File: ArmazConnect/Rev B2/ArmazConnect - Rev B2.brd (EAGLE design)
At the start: 165 x 74 mm, 37 parts, among them X0 NC3FAAV2, X1 NC3FAAV2, X2 NC3FAAV2, X3 NC3FAAV2, X4 NC5FAV-SW, X5 NC5MAV-SW, X6 NC5FAV-SW, X8 87832-26

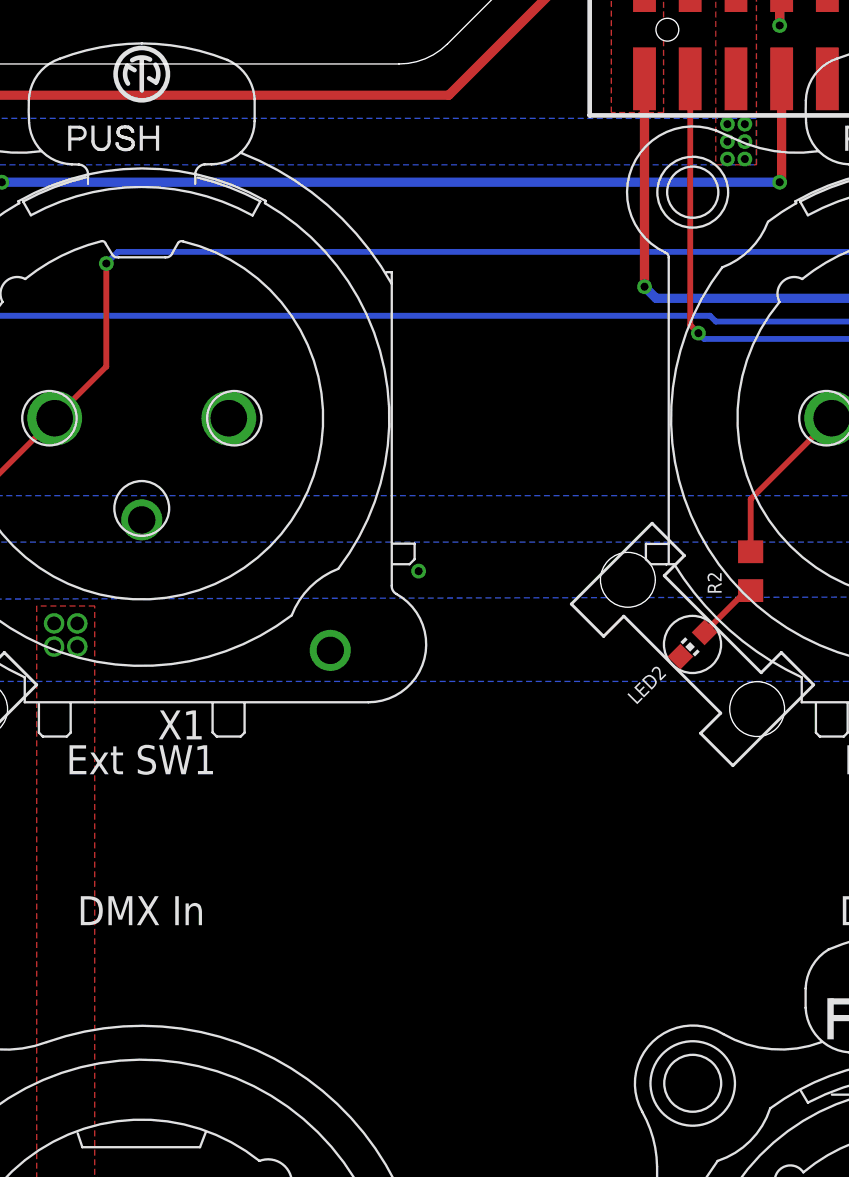
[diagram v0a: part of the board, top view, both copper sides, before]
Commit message: Update ArmazConnect - Rev B2 schematic and board, add two dc/dc converter (12V/5V) in parallel
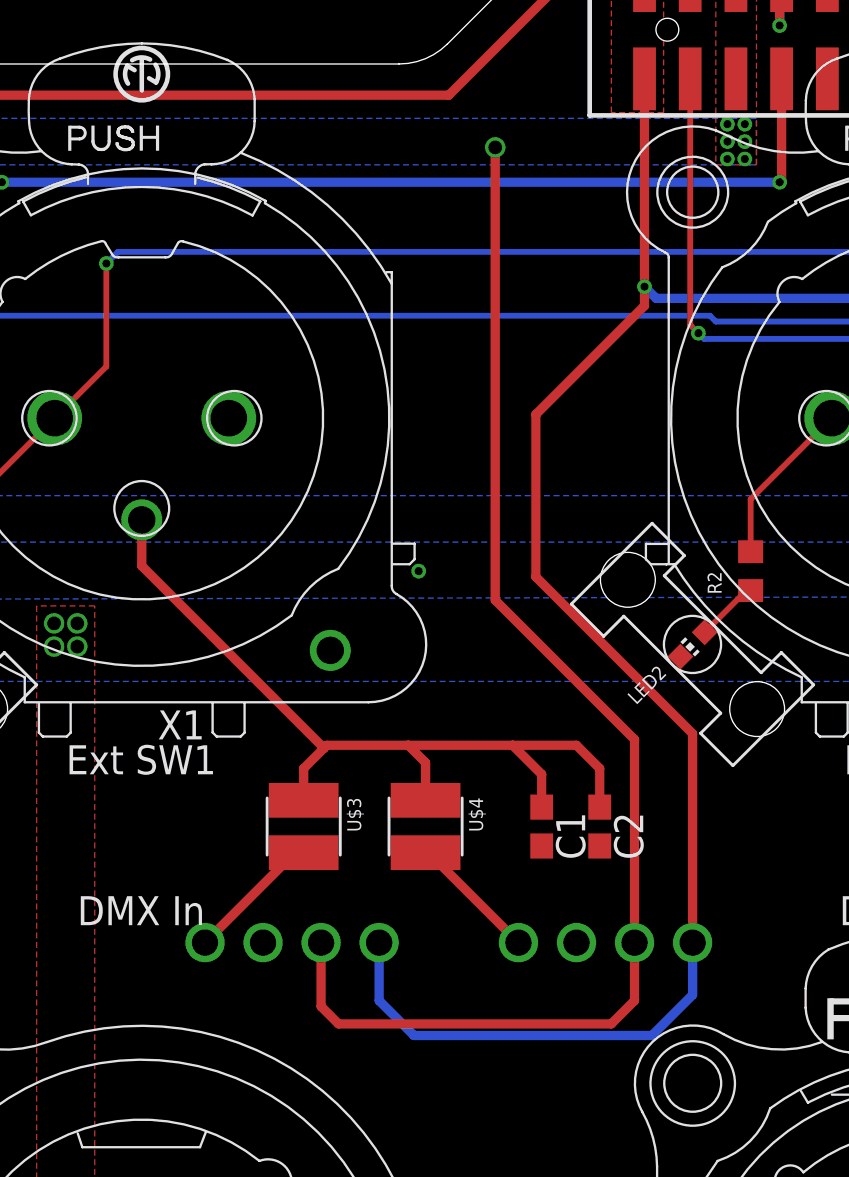
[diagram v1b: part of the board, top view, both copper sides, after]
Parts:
- added C1, C2: 4.7uF, rcl:C0603
- added U$1, U$2: MEE3S1205SC, dc-dc-converter:MEE3
- added U$3, U$4: 10uH, murata-inductance:8200
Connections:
- new net N$5: U$1.4, U$3.1
- new net N$7: U$2.4, U$4.1
- net +12V: now also U$1.2, U$2.2
- net +5V: now also C1.1, C2.1, U$3.2, U$4.2
- net GND: now also C1.2, C2.2, U$1.3, U$2.3
- net GND1: now also U$1.1, U$2.1
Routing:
- net +12V: track 0.00 -> 57.1 mm, vias 6 -> 7
- net GND1: track 79.3 -> 132.7 mm
- net +5V: track 33.5 -> 69.6 mm
- net N$5: track 0.00 -> 5.95 mm
- net N$7: track 0.00 -> 5.69 mm
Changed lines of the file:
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@@
 <attribute name="VALUE" x="136.906" y="57.912" size="0.4064" layer="27" ratio="10"/>
 </element>
+<element name="U$1" library="dc-dc-converter" package="MEE3" value="MEE3S1205SC" x="48.768" y="35.052" rot="MR0"/>
+<element name="U$2" library="dc-dc-converter" package="MEE3" value="MEE3S1205SC" x="62.484" y="35.052" rot="MR0"/>
+<element name="U$3" library="murata-inductance" package="8200" value="10uH" x="53.086" y="40.132" rot="R180"/>
+<element name="U$4" library="murata-inductance" package="8200" value="10uH" x="58.42" y="40.132" rot="R180"/>
+<element name="C1" library="rcl" package="C0603" value="4.7uF" x="63.5" y="40.132" rot="R270"/>
+<element name="C2" library="rcl" package="C0603" value="4.7uF" x="66.04" y="40.132" rot="R270"/>
 </elements>
 <signals>
@@
 <via x="118" y="45" extent="1-16" drill="0.35"/>
 <via x="135" y="45" extent="1-16" drill="0.35"/>
+<contactref element="C1" pad="2"/>
+<contactref element="C2" pad="2"/>
+<contactref element="U$2" pad="3"/>
+<contactref element="U$1" pad="3"/>
 </signal>
 <signal name="N$27">
@@
 <wire x1="137.414" y1="59.248" x2="137.8" y2="59.248" width="0.4064" layer="1"/>
 <wire x1="137.8" y1="59.248" x2="137.822" y2="59.27" width="0.4064" layer="1"/>
+<contactref element="U$3" pad="2"/>
+<contactref element="U$4" pad="2"/>
+<contactref element="C2" pad="1"/>
+<contactref element="C1" pad="1"/>
+<wire x1="53.086" y1="41.277" x2="53.086" y2="42.672" width="0.4064" layer="1"/>
+<wire x1="53.086" y1="42.672" x2="53.975" y2="43.561" width="0.4064" layer="1"/>
+<wire x1="53.975" y1="43.561" x2="54.102" y2="43.688" width="0.4064" layer="1"/>
+<wire x1="54.102" y1="43.688" x2="57.658" y2="43.688" width="0.4064" layer="1"/>
+<wire x1="57.658" y1="43.688" x2="62.23" y2="43.688" width="0.4064" layer="1"/>
+<wire x1="62.23" y1="43.688" x2="65.024" y2="43.688" width="0.4064" layer="1"/>
+<wire x1="65.024" y1="43.688" x2="66.04" y2="42.672" width="0.4064" layer="1"/>
+<wire x1="66.04" y1="42.672" x2="66.04" y2="40.982" width="0.4064" layer="1"/>
+<wire x1="63.5" y1="40.982" x2="63.5" y2="42.418" width="0.4064" layer="1"/>
+<wire x1="63.5" y1="42.418" x2="62.23" y2="43.688" width="0.4064" layer="1"/>
+<wire x1="58.42" y1="41.277" x2="58.42" y2="42.926" width="0.4064" layer="1"/>
+<wire x1="58.42" y1="42.926" x2="57.658" y2="43.688" width="0.4064" layer="1"/>
+<wire x1="46" y1="53.55" x2="46" y2="51.536" width="0.4064" layer="1"/>
+<wire x1="46" y1="51.536" x2="53.975" y2="43.561" width="0.4064" layer="1"/>
 </signal>
 <signal name="ESW0">
@@
 <via x="72.39" y="70.104" extent="1-16" drill="0.35" shape="square"/>
 <via x="71.628" y="70.104" extent="1-16" drill="0.35" shape="square"/>
+<contactref element="U$1" pad="2"/>
+<contactref element="U$2" pad="2"/>
+<wire x1="53.848" y1="35.052" x2="53.848" y2="32.258" width="0.4064" layer="1"/>
+<wire x1="53.848" y1="32.258" x2="54.61" y2="31.496" width="0.4064" layer="1"/>
+<wire x1="54.61" y1="31.496" x2="66.548" y2="31.496" width="0.4064" layer="1"/>
+<wire x1="66.548" y1="31.496" x2="67.564" y2="32.512" width="0.4064" layer="1"/>
+<wire x1="67.564" y1="32.512" x2="67.564" y2="35.052" width="0.4064" layer="1"/>
+<wire x1="67.564" y1="35.052" x2="67.564" y2="43.942" width="0.4064" layer="1"/>
+<wire x1="67.564" y1="43.942" x2="61.468" y2="50.038" width="0.4064" layer="1"/>
+<wire x1="61.468" y1="50.038" x2="61.468" y2="69.85" width="0.4064" layer="1"/>
+<via x="61.468" y="69.85" extent="1-16" drill="0.6" shape="square"/>
 </signal>
 <signal name="GND1" class="1">
@@
 <wire x1="68.508" y1="63.246" x2="68" y2="63.754" width="0.4064" layer="16"/>
 <via x="68" y="63.754" extent="1-16" drill="0.35"/>
+<contactref element="U$1" pad="1"/>
+<contactref element="U$2" pad="1"/>
+<wire x1="56.388" y1="35.052" x2="56.388" y2="32.512" width="0.4064" layer="16"/>
+<wire x1="56.388" y1="32.512" x2="57.912" y2="30.988" width="0.4064" layer="16"/>
+<wire x1="57.912" y1="30.988" x2="68.326" y2="30.988" width="0.4064" layer="16"/>
+<wire x1="68.326" y1="30.988" x2="70.104" y2="32.766" width="0.4064" layer="16"/>
+<wire x1="70.104" y1="32.766" x2="70.104" y2="35.052" width="0.4064" layer="16"/>
+<wire x1="70.104" y1="35.052" x2="70.104" y2="44.196" width="0.4064" layer="1"/>
+<wire x1="70.104" y1="44.196" x2="63.246" y2="51.054" width="0.4064" layer="1"/>
+<wire x1="63.246" y1="51.054" x2="63.246" y2="58.166" width="0.4064" layer="1"/>
+<wire x1="68" y1="63.754" x2="68" y2="62.92" width="0.4064" layer="1"/>
+<wire x1="68" y1="62.92" x2="63.246" y2="58.166" width="0.4064" layer="1"/>
 </signal>
 <signal name="FAN0_GND" class="1">
@@
 <wire x1="133.9224" y1="67.056" x2="134.0734" y2="66.905" width="0.254" layer="1"/>
 </signal>
+<signal name="N$5">
+<contactref element="U$1" pad="4"/>
+<contactref element="U$3" pad="1"/>
+<wire x1="53.086" y1="38.987" x2="52.703" y2="38.987" width="0.4064" layer="1"/>
+<wire x1="52.703" y1="38.987" x2="48.768" y2="35.052" width="0.4064" layer="1"/>
+</signal>
+<signal name="N$7">
+<contactref element="U$4" pad="1"/>
+<contactref element="U$2" pad="4"/>
+<wire x1="58.42" y1="38.987" x2="58.549" y2="38.987" width="0.4064" layer="1"/>
+<wire x1="58.549" y1="38.987" x2="62.484" y2="35.052" width="0.4064" layer="1"/>
+</signal>
 </signals>
